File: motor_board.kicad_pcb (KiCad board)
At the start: 2 copper layers, 100 x 90 mm, 36 parts, among them J1 MyRIO_C, J10 Conn_01x05, J11 Barrel_Jack_Switch, J12 Barrel_Jack_Switch, J2 BNC, J3 ESCON_24-2, J4 BNC, J5 Conn_01x08, J6 Conn_01x05, J7 Conn_01x05, J8 Conn_01x04, J9 Conn_01x02, SW1 SW_Push, SW2 SW_Push, U1 MC33063AP

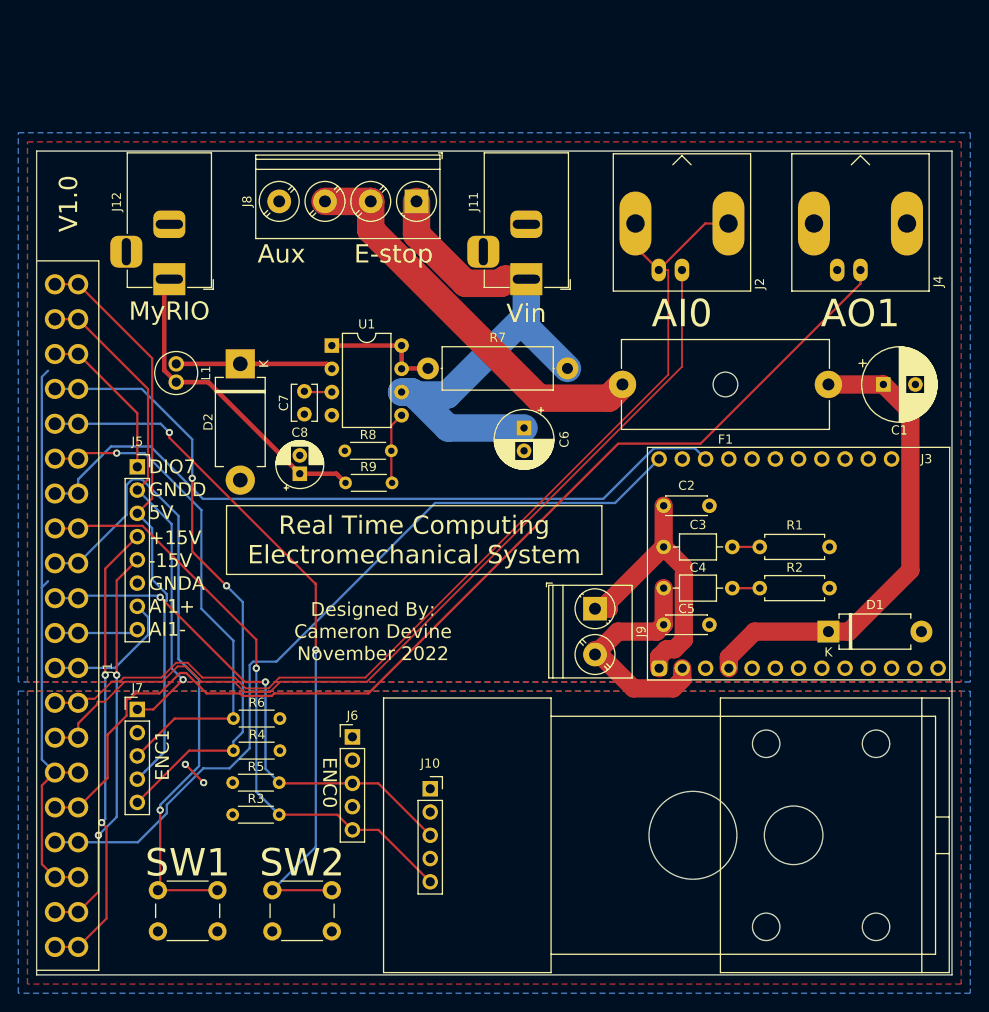
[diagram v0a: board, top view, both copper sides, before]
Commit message: removed the voltage regulator and shrunk the board
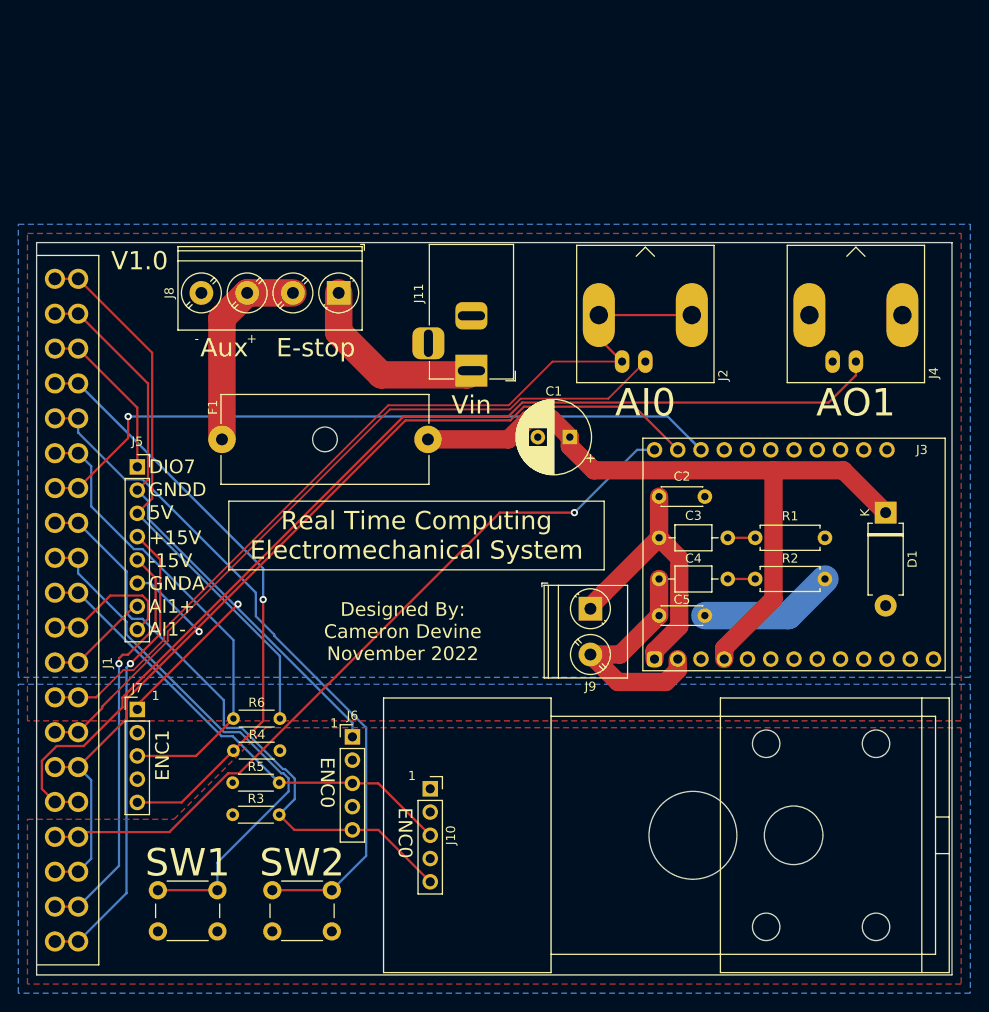
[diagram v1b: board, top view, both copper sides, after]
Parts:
- removed C6: 100uF, Capacitor_THT:CP_Radial_D6.3mm_P2.50mm
- removed C7: 68pF, Capacitor_THT:C_Disc_D3.8mm_W2.6mm_P2.50mm
- removed C8: 39uF, Capacitor_THT:CP_Radial_D5.0mm_P2.00mm
- removed D2: 1N5822, Diode_THT:D_DO-201AD_P12.70mm_Horizontal
- removed J12: Barrel_Jack_Switch, Connector_BarrelJack:BarrelJack_Horizontal
- removed L1: 1uH, motor_board:L_Radial_D5.0mm_P2.00mm
- removed R7: 0.1, Resistor_THT:R_Axial_DIN0414_L11.9mm_D4.5mm_P15.24mm_Horizontal
- removed R8: 1k, Resistor_THT:R_Axial_DIN0204_L3.6mm_D1.6mm_P5.08mm_Horizontal
- removed R9: 6.2k, Resistor_THT:R_Axial_DIN0204_L3.6mm_D1.6mm_P5.08mm_Horizontal
- removed U1: MC33063AP, Package_DIP:DIP-8_W7.62mm
- moved F1 44.2 mm to (80.8, 79.5)
- moved C1 34.7 mm to (96.2, 79.2), turned to 180 degrees
- moved D1 14.4 mm to (130.8, 87.5), turned to 270 degrees
- moved J8 13.1 mm to (71.0, 63.5)
- moved J11 11.7 mm to (85.5, 72.0)
- moved J2 10.8 mm to (104.5, 71.0)
- moved J4 10.0 mm to (127.5, 71.0)
- moved C2 1.12 mm to (106.0, 85.8)
- moved C3 1.12 mm to (106.0, 90.2)
- moved C4 1.12 mm to (106.0, 94.8)
- moved C5 1.12 mm to (106.0, 98.8)
- moved J3 1.12 mm to (105.5, 103.5)
- moved R1 1.12 mm to (116.5, 90.2)
- moved R2 1.12 mm to (116.5, 94.8)
- moved J1 0.59 mm to (38.0, 98.2)
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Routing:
- net GNDA: track 63.9 -> 112.5 mm, vias 0 -> 1
- net VIN: track 62.0 -> 20.9 mm
- net 9V: track 35.1 -> 0.00 mm
- net Net-(C1-Pad1): track 52.5 -> 78.6 mm
- net GNDD: track 54.0 -> 78.5 mm
- net VBUS: track 43.9 -> 22.1 mm
- net /AI0-: track 112.5 -> 94.1 mm
- net /AI0+: track 99.2 -> 82.0 mm
- net Net-(D2-Pad1): track 17.2 -> 0.00 mm
- net GNDPWR: track 0.00 -> 14.8 mm
- net Net-(R7-Pad1): track 13.1 -> 0.00 mm
- net /BUT1: track 71.1 -> 59.3 mm, vias 1 -> 0
- net Net-(R8-Pad2): track 7.88 -> 0.00 mm
- net /AI1-: track 9.16 -> 15.5 mm
- net /CUR: track 89.2 -> 83.0 mm, vias 0 -> 1
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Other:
- board size 100 x 90 mm -> 100 x 80 mm
- board text added: "+"
- board text added: "-"
- board text added: "1"
- board text removed: "MyRIO"

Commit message: changed the switch labels and moved some things around
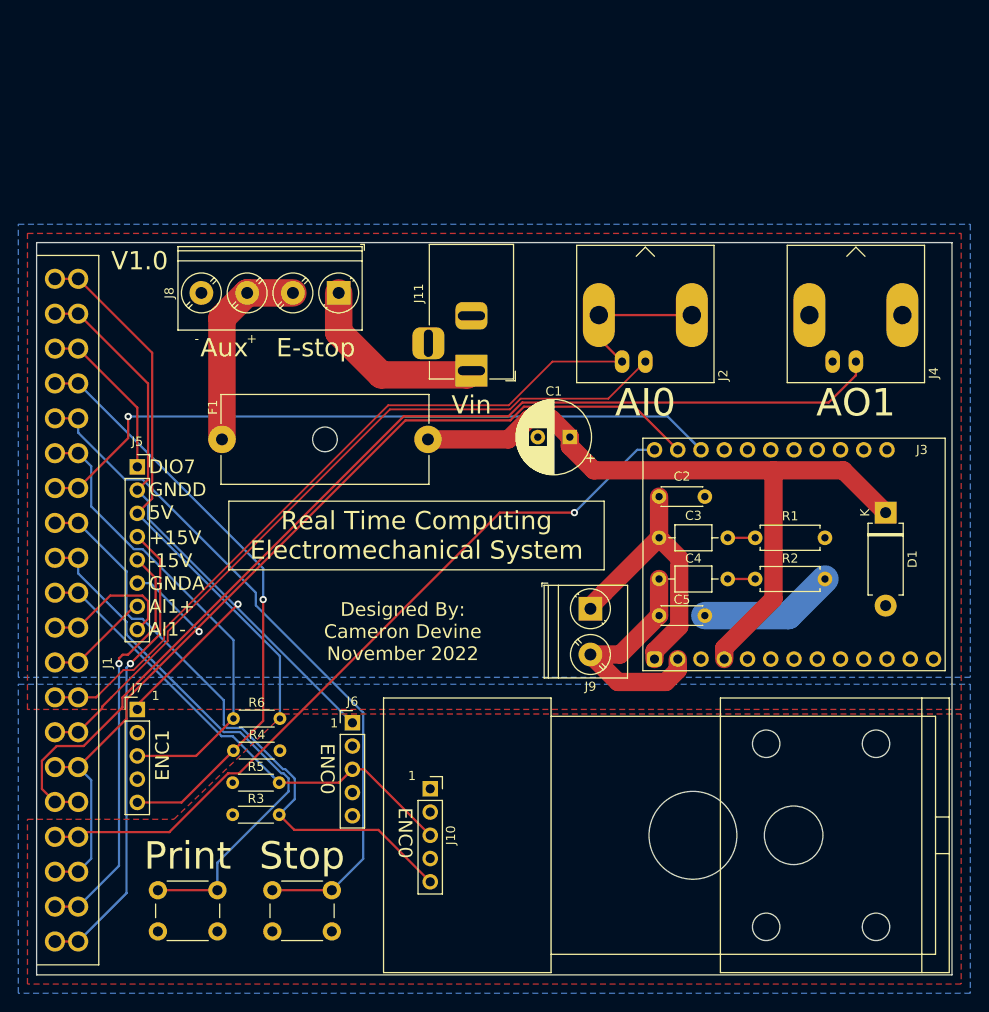
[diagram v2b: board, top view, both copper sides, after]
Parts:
- removed SW1: SW_Push, Button_Switch_THT:SW_PUSH_6mm_H5mm
- added Print: SW_Push, Button_Switch_THT:SW_PUSH_6mm_H5mm, F.Cu at (51.2, 128.8)
- moved J6 1.54 mm to (72.5, 110.5)
- renumbered SW2 to Stop
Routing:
- net GNDD: track 78.5 -> 77.0 mm
- net /ENC0.A: track 52.0 -> 53.2 mm

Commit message: added TVS diodes for safety
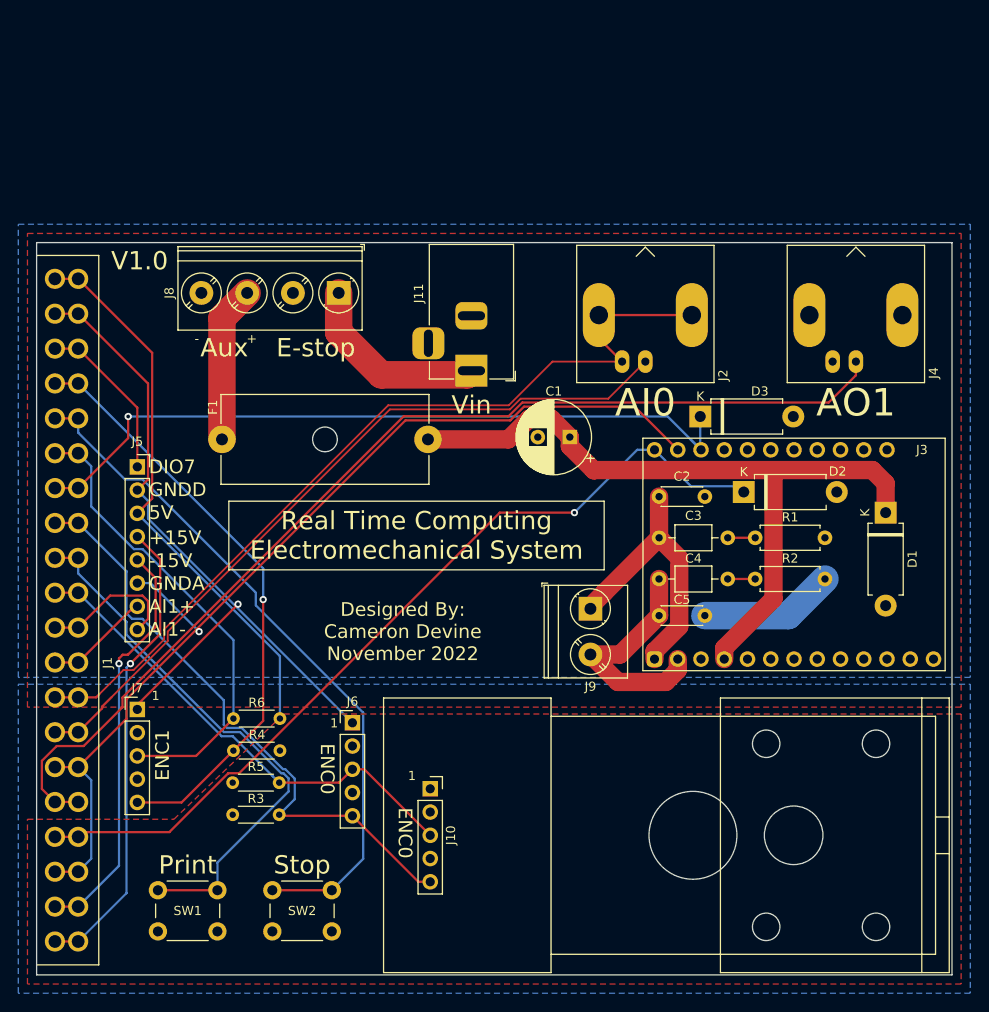
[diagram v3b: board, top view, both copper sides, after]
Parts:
- removed Print, Stop: SW_Push, Button_Switch_THT:SW_PUSH_6mm_H5mm
- added D2: D_TVS, Diode_THT:D_DO-15_P10.16mm_Horizontal, F.Cu at (115.2, 85.2)
- added D3: D_TVS, Diode_THT:D_DO-15_P10.16mm_Horizontal, F.Cu at (110.5, 77.0)
- added SW1: SW_Push, Button_Switch_THT:SW_PUSH_6mm_H5mm, F.Cu at (51.2, 128.8)
- added SW2: SW_Push, Button_Switch_THT:SW_PUSH_6mm_H5mm, F.Cu at (63.8, 128.8)
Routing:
- net /CUR: track 83.0 -> 94.7 mm
- net VBUS: track 22.1 -> 17.1 mm
- net /PWM: track 78.4 -> 82.0 mm
- net Net-(C1-Pad1): track 78.6 -> 80.5 mm
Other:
- board text added: "Print"
- board text added: "Stop"

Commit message: twisted the motor and added a couple connectors
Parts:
- added J12: BNC, Connector_Coaxial:BNC_Amphenol_B6252HB-NPP3G-50_Horizontal, F.Cu at (46.5, 56.0)
- added JP1: Jumper_2_Bridged, Connector_PinHeader_2.54mm:PinHeader_1x02_P2.54mm_Vertical, F.Cu at (95.5, 110.0)
- added TP1: TestPoint, TestPoint:TestPoint_Pad_D2.0mm, F.Cu at (95.8, 92.2)
- added TP2: TestPoint, TestPoint:TestPoint_Pad_D2.0mm, F.Cu at (95.8, 96.2)
- added TP3: TestPoint, TestPoint:TestPoint_Pad_D2.0mm, F.Cu at (95.8, 100.3)
- moved J10 57.2 mm to (119.5, 80.5), turned to 270 degrees
- moved D1 52.7 mm to (81.0, 104.8), turned to 180 degrees
- moved J8 51.7 mm to (120.5, 48.5)
- moved J11 48.5 mm to (131.8, 57.2)
- moved J3 47.1 mm to (65.0, 79.5), turned to 90 degrees
- moved D3 45.2 mm to (86.9, 115.5), turned to 180 degrees
- moved R2 43.0 mm to (73.8, 90.5), turned to 270 degrees
- moved C5 40.8 mm to (69.8, 80.0), turned to 270 degrees
- moved R1 38.3 mm to (78.2, 90.5), turned to 270 degrees
- moved J2 38.1 mm to (69.5, 56.0)
- moved J4 38.1 mm to (92.5, 56.0)
- moved C4 35.5 mm to (73.8, 80.0), turned to 270 degrees
- moved D2 32.2 mm to (83.2, 89.2), turned to 270 degrees
- moved C3 29.6 mm to (78.2, 80.0), turned to 270 degrees
- moved F1 25.6 mm to (102.8, 66.5), turned to 0 degrees
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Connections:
- J3 pad 17: (no net) -> Net-(J3-Pad17)
- J3 pad 19: (no net) -> Net-(J3-Pad19)
- J3 pad 20: (no net) -> Net-(J3-Pad20)
- J3 pad 6: (no net) -> /+5
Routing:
- net GNDA: track 112.5 -> 0.00 mm, vias 1 -> 0
- net /ENC0.A: track 53.2 -> 138.9 mm
- net /ENC0.B: track 66.2 -> 148.2 mm, vias 0 -> 1
- net GNDD: track 77.0 -> 158.4 mm, vias 1 -> 2
- net /+5: track 0.00 -> 39.3 mm
- net /PWM: track 82.0 -> 120.4 mm, vias 1 -> 2
- net /AO1: track 116.1 -> 90.7 mm
- net /CUR: track 94.7 -> 77.3 mm, vias 1 -> 0
- net Net-(J3-Pad17): track 0.00 -> 16.9 mm
- net /M+: track 29.9 -> 44.4 mm
- net /AI0-: track 94.1 -> 80.2 mm
- net /AI0+: track 82.0 -> 69.2 mm
- net /BUT2: track 76.0 -> 88.1 mm, vias 0 -> 1
- net /-15V: track 45.1 -> 55.5 mm, vias 1 -> 2
- net VBUS: track 17.1 -> 27.0 mm
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- added copper zone on F.Cu, net 5V
- removed copper zone on B.Cu, net 5V
- removed copper zone on F.Cu, net GNDD
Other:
- board size 100 x 80 mm -> 100 x 94.2 mm
- net class Input Power: trace_width 3 -> 2.5
- board text added: "AO2"
- board text added: "Enable"
- board text added: "GND"
- board text added: "PWM"

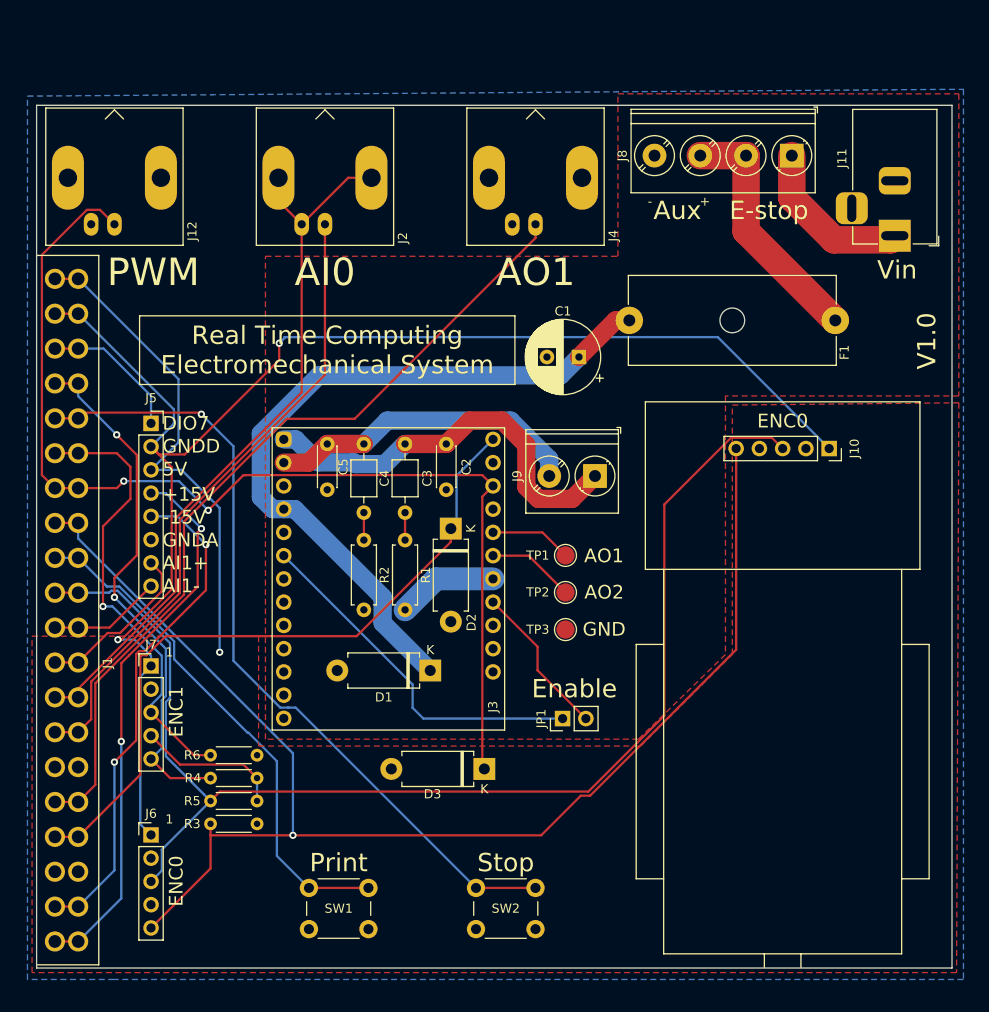
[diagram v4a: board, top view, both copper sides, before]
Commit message: renumbered components
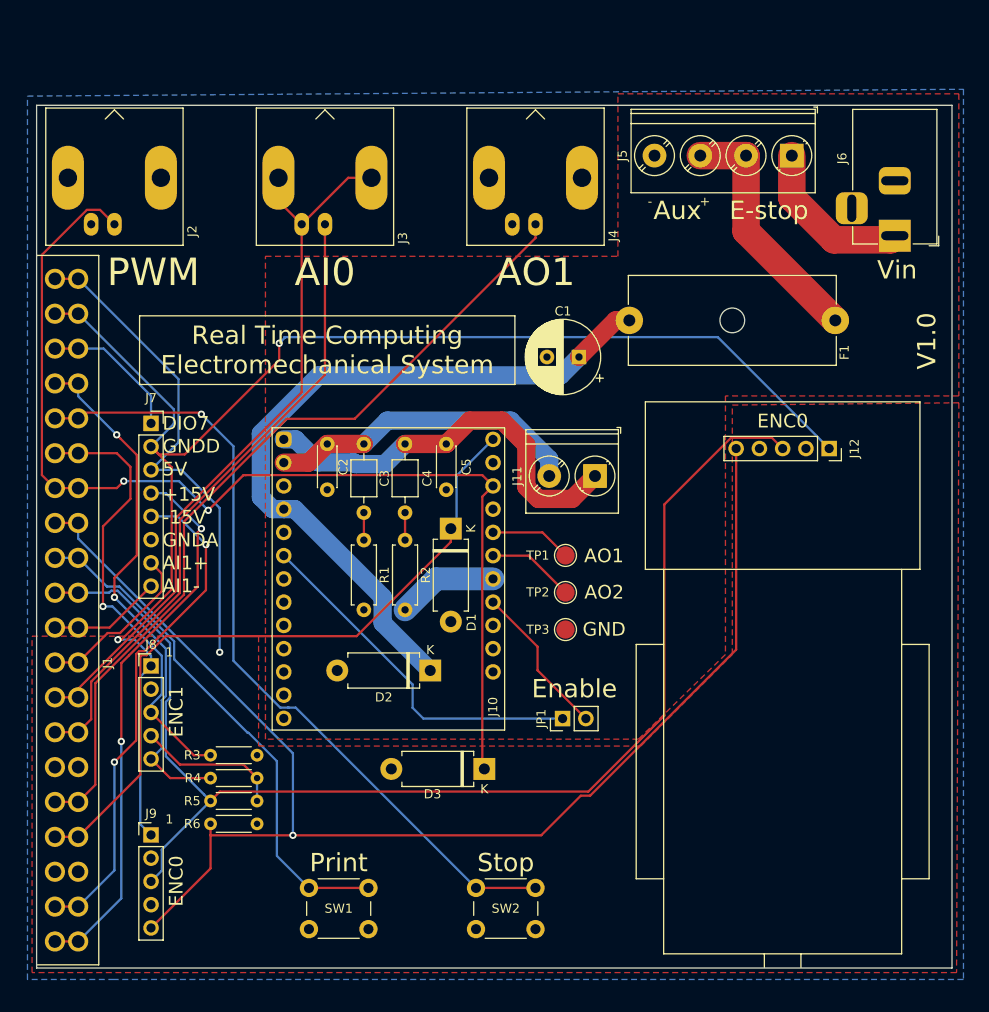
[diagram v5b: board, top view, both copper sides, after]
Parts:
- renumbered C5 to C2, C4 to C3, C3 to C4, C2 to C5, D2 to D1, D1 to D2, J3 to J10, J9 to J11, J10 to J12, J12 to J2, J2 to J3, J8 to J5, J11 to J6, J5 to J7, J7 to J8, J6 to J9, R2 to R1, R1 to R2, R6 to R3, R3 to R6

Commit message: changed date
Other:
- board text added: "Designed By: Cameron Devine April 2023"
- board text removed: "Designed By: Cameron Devine November 2022"
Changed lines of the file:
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@@
   (gr_line (start 49.25 73.5) (end 90.25 73.5) (layer F.SilkS) (width 0.12))
   (gr_line (start 49.25 66) (end 49.25 73.5) (layer F.SilkS) (width 0.12))
-  (gr_text "Designed By:\nCameron Devine\nNovember 2022" (at 69.75 66.5) (layer B.SilkS)
+  (gr_text "Designed By:\nCameron Devine\nApril 2023" (at 69.75 66.5) (layer B.SilkS)
     (effects (font (size 1.5 1.5) (thickness 0.22)) (justify mirror))
   )

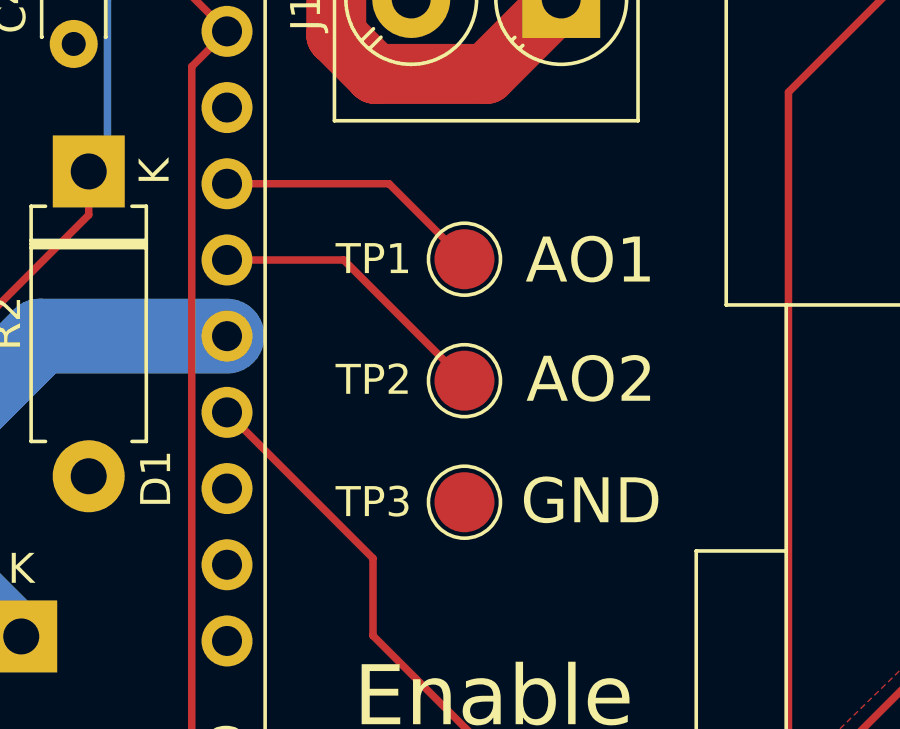
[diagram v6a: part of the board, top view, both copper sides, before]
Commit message: change test points to pin sockets
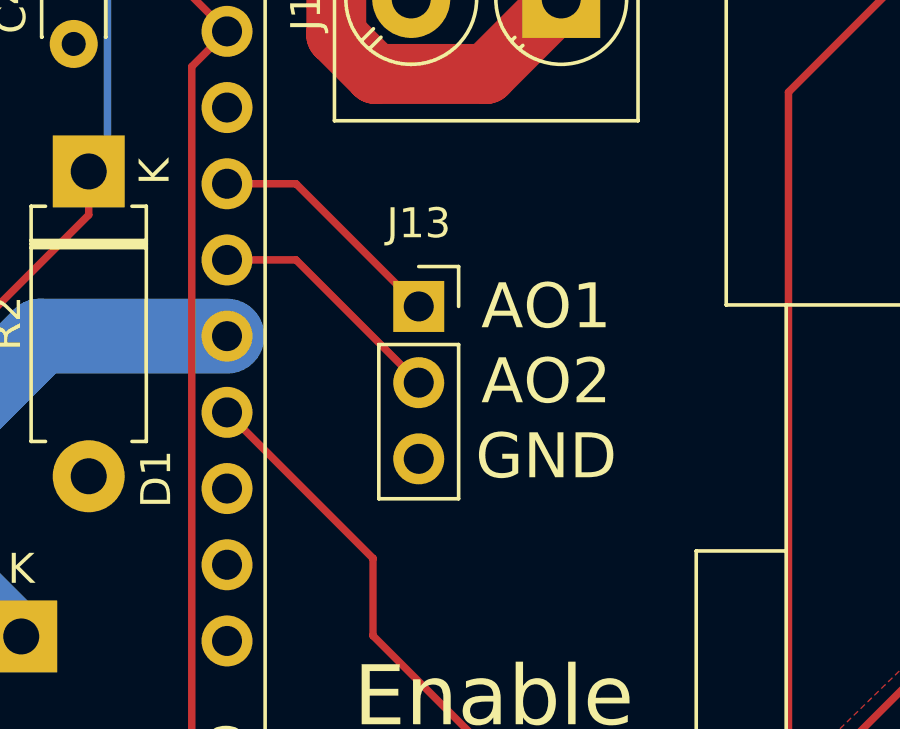
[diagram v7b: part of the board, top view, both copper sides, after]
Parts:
- removed TP1, TP2, TP3: TestPoint, TestPoint:TestPoint_Pad_D2.0mm
- added J13: Conn_01x03, Connector_PinSocket_2.54mm:PinSocket_1x03_P2.54mm_Vertical, F.Cu at (94.2, 93.8)
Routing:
- net Net-(J10-Pad19): track 9.58 -> 8.08 mm
- net Net-(J10-Pad20): track 8.96 -> 8.08 mm
